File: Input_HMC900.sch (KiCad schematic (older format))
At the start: 8 parts

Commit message: As implemented for v1
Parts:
- R23: value 0 -> 0(NP)
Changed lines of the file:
@@
 AR Path="/60D21B6E/61121120/60F9EBFF" Ref="C28"  Part="1"
 AR Path="/60D21B6E/60F52DEE/60F9EBFF" Ref="C30"  Part="1"
-F 0 "C30" H 6150 2800 50  0000 R CNN
+F 0 "C28" H 6150 2800 50  0000 R CNN
 F 1 "100p" H 6175 3000 50  0000 R CNN
 F 2 "Capacitor_SMD:C_0603_1608Metric_Pad1.08x0.95mm_HandSolder" H 6238 2750 50  0001 C CNN
@@
 AR Path="/60D21B6E/61121120/60F9EC14" Ref="#PWR0131"  Part="1"
 AR Path="/60D21B6E/60F52DEE/60F9EC14" Ref="#PWR0135"  Part="1"
-F 0 "#PWR0135" H 6200 2850 50  0001 C CNN
+F 0 "#PWR0131" H 6200 2850 50  0001 C CNN
 F 1 "GND" H 6205 2927 50  0000 C CNN
 F 2 "" H 6200 3100 50  0001 C CNN
@@
 AR Path="/60D21B6E/61121120/60F9EC05" Ref="C29"  Part="1"
 AR Path="/60D21B6E/60F52DEE/60F9EC05" Ref="C31"  Part="1"
-F 0 "C31" H 6450 2800 50  0000 R CNN
+F 0 "C29" H 6450 2800 50  0000 R CNN
 F 1 "100p" H 6475 3000 50  0000 R CNN
 F 2 "Capacitor_SMD:C_0603_1608Metric_Pad1.08x0.95mm_HandSolder" H 6538 2750 50  0001 C CNN
@@
 AR Path="/60D21B6E/61121120/6100BC4B" Ref="#PWR0134"  Part="1"
 AR Path="/60D21B6E/60F52DEE/6100BC4B" Ref="#PWR0136"  Part="1"
-F 0 "#PWR0136" H 6500 2850 50  0001 C CNN
+F 0 "#PWR0134" H 6500 2850 50  0001 C CNN
 F 1 "GND" H 6505 2927 50  0000 C CNN
 F 2 "" H 6500 3100 50  0001 C CNN
@@
 AR Path="/60D21B6E/61121120/60F9EBF5" Ref="R32"  Part="1"
 AR Path="/60D21B6E/60F52DEE/60F9EBF5" Ref="R33"  Part="1"
-F 0 "R33" H 5920 2946 50  0000 L CNN
+F 0 "R32" H 5920 2946 50  0000 L CNN
 F 1 "51" H 5920 2855 50  0000 L CNN
 F 2 "Resistor_SMD:R_0603_1608Metric_Pad0.98x0.95mm_HandSolder" V 5780 2900 50  0001 C CNN
@@
 AR Path="/60D21B6E/61121120/60F9EC23" Ref="R31"  Part="1"
 AR Path="/60D21B6E/60F52DEE/60F9EC23" Ref="R34"  Part="1"
-F 0 "R34" H 5620 2946 50  0000 L CNN
+F 0 "R31" H 5620 2946 50  0000 L CNN
 F 1 "51" H 5620 2855 50  0000 L CNN
 F 2 "Resistor_SMD:R_0603_1608Metric_Pad0.98x0.95mm_HandSolder" V 5480 2900 50  0001 C CNN
@@
 AR Path="/60D21B6E/61121120/60F9EC42" Ref="#PWR0133"  Part="1"
 AR Path="/60D21B6E/60F52DEE/60F9EC42" Ref="#PWR0137"  Part="1"
-F 0 "#PWR0137" H 4900 3650 50  0001 C CNN
+F 0 "#PWR0133" H 4900 3650 50  0001 C CNN
 F 1 "GND" H 4905 3727 50  0000 C CNN
 F 2 "" H 4900 3900 50  0001 C CNN
@@
 AR Path="/60D21B6E/61121120/60F9EC6C" Ref="C45"  Part="1"
 AR Path="/60D21B6E/60F52DEE/60F9EC6C" Ref="C46"  Part="1"
-F 0 "C46" H 4785 3654 50  0000 R CNN
+F 0 "C45" H 4785 3654 50  0000 R CNN
 F 1 "10µ" H 4785 3745 50  0000 R CNN
 F 2 "Capacitor_SMD:C_0603_1608Metric_Pad1.08x0.95mm_HandSolder" H 4938 3550 50  0001 C CNN
@@
 AR Path="/60D21B6E/60F52DEE/60F9EC66" Ref="TR4"  Part="1"
 AR Path="/60F9EC66" Ref="TR4"  Part="1"
-F 0 "TR4" H 4250 3881 50  0000 C CNN
+F 0 "TR3" H 4250 3881 50  0000 C CNN
 F 1 "ADT2-1T" H 4250 3790 50  0000 C CNN
 F 2 "RF_Mini-Circuits:Mini-Circuits_CD542_H2.84mm" H 4250 3150 50  0001 C CNN
@@
 AR Path="/60D21B6E/61121120/614655FD" Ref="R23"  Part="1"
 AR Path="/60D21B6E/60F52DEE/614655FD" Ref="R26"  Part="1"
-F 0 "R26" H 3870 3346 50  0000 L CNN
-F 1 "0" V 3800 3250 50  0000 L CNN
+F 0 "R23" H 3870 3346 50  0000 L CNN
+F 1 "0(NP)" V 3800 3200 50  0000 L CNN
 F 2 "Resistor_SMD:R_0603_1608Metric_Pad0.98x0.95mm_HandSolder" V 3730 3300 50  0001 C CNN
 F 3 "~" H 3800 3300 50  0001 C CNN
@@
 AR Path="/60D21B6E/61121120/6147240B" Ref="R22"  Part="1"
 AR Path="/60D21B6E/60F52DEE/6147240B" Ref="R25"  Part="1"
-F 0 "R25" H 4070 3146 50  0000 L CNN
+F 0 "R22" H 4070 3146 50  0000 L CNN
 F 1 "0" V 4000 3050 50  0000 L CNN
 F 2 "Resistor_SMD:R_0603_1608Metric_Pad0.98x0.95mm_HandSolder" V 3930 3100 50  0001 C CNN
@@
 AR Path="/60D21B6E/61121120/614747AB" Ref="#PWR09"  Part="1"
 AR Path="/60D21B6E/60F52DEE/614747AB" Ref="#PWR010"  Part="1"
-F 0 "#PWR010" H 3800 2750 50  0001 C CNN
+F 0 "#PWR09" H 3800 2750 50  0001 C CNN
 F 1 "GND" H 3805 2827 50  0000 C CNN
 F 2 "" H 3800 3000 50  0001 C CNN

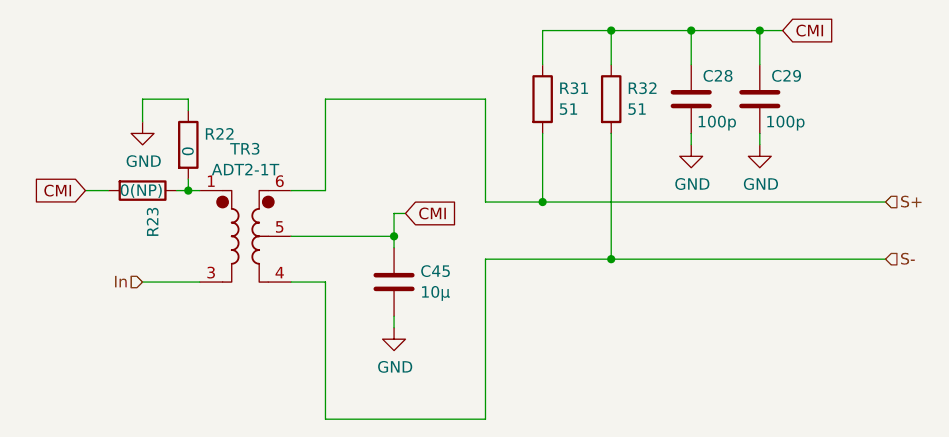
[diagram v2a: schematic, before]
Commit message: removed unused options added aop at the output
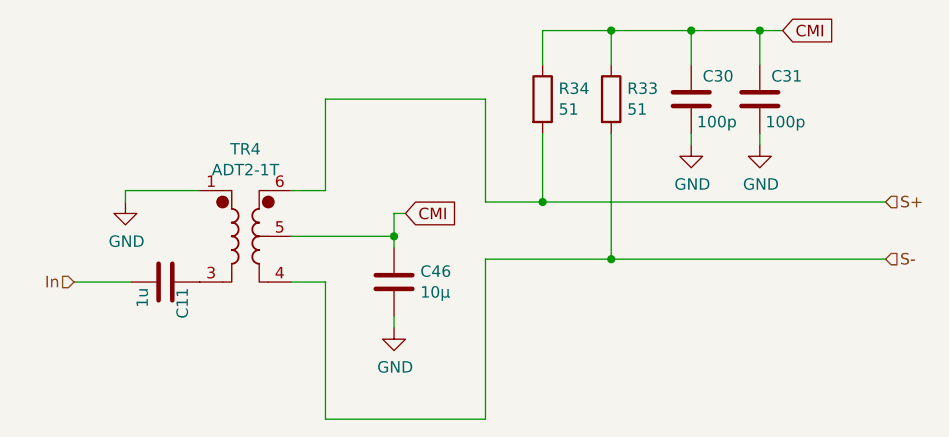
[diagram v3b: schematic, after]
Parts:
- removed R22: 0, Resistor_SMD:R_0603_1608Metric_Pad0.98x0.95mm_HandSolder, symbol Device:R
- removed R23: 0(NP), Resistor_SMD:R_0603_1608Metric_Pad0.98x0.95mm_HandSolder, symbol Device:R
- added C10: 1u, Capacitor_SMD:C_0603_1608Metric_Pad1.08x0.95mm_HandSolder, symbol Device:C
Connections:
- net GND: now also TR4.1
- net In: now also C10.1; no longer TR4.3
- new net: C10.2, TR4.3
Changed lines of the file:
@@
 AR Path="/60D21B6E/61121120/60F9EBFF" Ref="C28"  Part="1"
 AR Path="/60D21B6E/60F52DEE/60F9EBFF" Ref="C30"  Part="1"
-F 0 "C28" H 6150 2800 50  0000 R CNN
+F 0 "C30" H 6150 2800 50  0000 R CNN
 F 1 "100p" H 6175 3000 50  0000 R CNN
 F 2 "Capacitor_SMD:C_0603_1608Metric_Pad1.08x0.95mm_HandSolder" H 6238 2750 50  0001 C CNN
@@
 AR Path="/60D21B6E/61121120/60F9EC14" Ref="#PWR0131"  Part="1"
 AR Path="/60D21B6E/60F52DEE/60F9EC14" Ref="#PWR0135"  Part="1"
-F 0 "#PWR0131" H 6200 2850 50  0001 C CNN
+F 0 "#PWR0135" H 6200 2850 50  0001 C CNN
 F 1 "GND" H 6205 2927 50  0000 C CNN
 F 2 "" H 6200 3100 50  0001 C CNN
@@
 AR Path="/60D21B6E/61121120/60F9EC05" Ref="C29"  Part="1"
 AR Path="/60D21B6E/60F52DEE/60F9EC05" Ref="C31"  Part="1"
-F 0 "C29" H 6450 2800 50  0000 R CNN
+F 0 "C31" H 6450 2800 50  0000 R CNN
 F 1 "100p" H 6475 3000 50  0000 R CNN
 F 2 "Capacitor_SMD:C_0603_1608Metric_Pad1.08x0.95mm_HandSolder" H 6538 2750 50  0001 C CNN
@@
 AR Path="/60D21B6E/61121120/6100BC4B" Ref="#PWR0134"  Part="1"
 AR Path="/60D21B6E/60F52DEE/6100BC4B" Ref="#PWR0136"  Part="1"
-F 0 "#PWR0134" H 6500 2850 50  0001 C CNN
+F 0 "#PWR0136" H 6500 2850 50  0001 C CNN
 F 1 "GND" H 6505 2927 50  0000 C CNN
 F 2 "" H 6500 3100 50  0001 C CNN
@@
 Wire Wire Line
 	5850 3600 7050 3600
-Text HLabel 3800 3700 0    50   Input ~ 0
+Text HLabel 3500 3700 0    50   Input ~ 0
 In
 Text HLabel 7050 3350 2    50   Input ~ 0
@@
 AR Path="/60D21B6E/61121120/60F9EBF5" Ref="R32"  Part="1"
 AR Path="/60D21B6E/60F52DEE/60F9EBF5" Ref="R33"  Part="1"
-F 0 "R32" H 5920 2946 50  0000 L CNN
+F 0 "R33" H 5920 2946 50  0000 L CNN
 F 1 "51" H 5920 2855 50  0000 L CNN
 F 2 "Resistor_SMD:R_0603_1608Metric_Pad0.98x0.95mm_HandSolder" V 5780 2900 50  0001 C CNN
@@
 AR Path="/60D21B6E/61121120/60F9EC23" Ref="R31"  Part="1"
 AR Path="/60D21B6E/60F52DEE/60F9EC23" Ref="R34"  Part="1"
-F 0 "R31" H 5620 2946 50  0000 L CNN
+F 0 "R34" H 5620 2946 50  0000 L CNN
 F 1 "51" H 5620 2855 50  0000 L CNN
 F 2 "Resistor_SMD:R_0603_1608Metric_Pad0.98x0.95mm_HandSolder" V 5480 2900 50  0001 C CNN
@@
 AR Path="/60D21B6E/61121120/60F9EC42" Ref="#PWR0133"  Part="1"
 AR Path="/60D21B6E/60F52DEE/60F9EC42" Ref="#PWR0137"  Part="1"
-F 0 "#PWR0133" H 4900 3650 50  0001 C CNN
+F 0 "#PWR0137" H 4900 3650 50  0001 C CNN
 F 1 "GND" H 4905 3727 50  0000 C CNN
 F 2 "" H 4900 3900 50  0001 C CNN
@@
 Wire Wire Line
 	4900 3500 4900 3550
-Wire Wire Line
-	4050 3300 4000 3300
 $Comp
 L Device:C C?
@@
 AR Path="/60D21B6E/61121120/60F9EC6C" Ref="C45"  Part="1"
 AR Path="/60D21B6E/60F52DEE/60F9EC6C" Ref="C46"  Part="1"
-F 0 "C45" H 4785 3654 50  0000 R CNN
+F 0 "C46" H 4785 3654 50  0000 R CNN
 F 1 "10µ" H 4785 3745 50  0000 R CNN
 F 2 "Capacitor_SMD:C_0603_1608Metric_Pad1.08x0.95mm_HandSolder" H 4938 3550 50  0001 C CNN
@@
 AR Path="/60D21B6E/60F52DEE/60F9EC66" Ref="TR4"  Part="1"
 AR Path="/60F9EC66" Ref="TR4"  Part="1"
-F 0 "TR3" H 4250 3881 50  0000 C CNN
+F 0 "TR4" H 4250 3881 50  0000 C CNN
 F 1 "ADT2-1T" H 4250 3790 50  0000 C CNN
 F 2 "RF_Mini-Circuits:Mini-Circuits_CD542_H2.84mm" H 4250 3150 50  0001 C CNN
@@
 Connection ~ 5550 3350
 Wire Wire Line
-	3800 3700 4050 3700
+	3500 3700 3750 3700
 Wire Wire Line
 	4450 3300 4600 3300
@@
 Wire Wire Line
 	4600 4300 5300 4300
-Text GLabel 3550 3300 0    50   Input ~ 0
-CMI
-$Comp
-L Device:R R?
-U 1 1 614655FD
-P 3800 3300
-AR Path="/60D21B6E/614655FD" Ref="R?"  Part="1"
-AR Path="/60D21B6E/60D894BC/614655FD" Ref="R?"  Part="1"
-AR Path="/60D21B6E/6110419F/614655FD" Ref="R?"  Part="1"
-AR Path="/60D21B6E/61121120/614655FD" Ref="R23"  Part="1"
-AR Path="/60D21B6E/60F52DEE/614655FD" Ref="R26"  Part="1"
-F 0 "R23" H 3870 3346 50  0000 L CNN
-F 1 "0(NP)" V 3800 3200 50  0000 L CNN
-F 2 "Resistor_SMD:R_0603_1608Metric_Pad0.98x0.95mm_HandSolder" V 3730 3300 50  0001 C CNN
-F 3 "~" H 3800 3300 50  0001 C CNN
-	1    3800 3300
-	0    1    1    0
-$EndComp
-Wire Wire Line
-	3650 3300 3550 3300
-$Comp
-L Device:R R?
-U 1 1 6147240B
-P 4000 3100
-AR Path="/60D21B6E/6147240B" Ref="R?"  Part="1"
-AR Path="/60D21B6E/60D894BC/6147240B" Ref="R?"  Part="1"
-AR Path="/60D21B6E/6110419F/6147240B" Ref="R?"  Part="1"
-AR Path="/60D21B6E/61121120/6147240B" Ref="R22"  Part="1"
-AR Path="/60D21B6E/60F52DEE/6147240B" Ref="R25"  Part="1"
-F 0 "R22" H 4070 3146 50  0000 L CNN
-F 1 "0" V 4000 3050 50  0000 L CNN
-F 2 "Resistor_SMD:R_0603_1608Metric_Pad0.98x0.95mm_HandSolder" V 3930 3100 50  0001 C CNN
-F 3 "~" H 4000 3100 50  0001 C CNN
-	1    4000 3100
-	1    0    0    -1
-$EndComp
 $Comp
 L power:GND #PWR?
 U 1 1 614747AB
-P 3800 3000
+P 3725 3350
 AR Path="/60D21B6E/614747AB" Ref="#PWR?"  Part="1"
 AR Path="/60D21B6E/60D894BC/614747AB" Ref="#PWR?"  Part="1"
@@
 AR Path="/60D21B6E/61121120/614747AB" Ref="#PWR09"  Part="1"
 AR Path="/60D21B6E/60F52DEE/614747AB" Ref="#PWR010"  Part="1"
-F 0 "#PWR09" H 3800 2750 50  0001 C CNN
-F 1 "GND" H 3805 2827 50  0000 C CNN
-F 2 "" H 3800 3000 50  0001 C CNN
-F 3 "" H 3800 3000 50  0001 C CNN
-	1    3800 3000
-	1    0    0    -1
-$EndComp
-Wire Wire Line
-	3800 2900 4000 2900
-Wire Wire Line
-	4000 2900 4000 2950
-Wire Wire Line
-	3800 2900 3800 3000
-Wire Wire Line
-	4000 3250 4000 3300
-Connection ~ 4000 3300
-Wire Wire Line
-	4000 3300 3950 3300
+F 0 "#PWR010" H 3725 3100 50  0001 C CNN
+F 1 "GND" H 3730 3177 50  0000 C CNN
+F 2 "" H 3725 3350 50  0001 C CNN
+F 3 "" H 3725 3350 50  0001 C CNN
+	1    3725 3350
+	1    0    0    -1
+$EndComp
+Wire Wire Line
+	3725 3300 3725 3350
+Wire Wire Line
+	3725 3300 4050 3300
+$Comp
+L Device:C C?
+U 1 1 616D127D
+P 3900 3700
+AR Path="/60D21B6E/616D127D" Ref="C?"  Part="1"
+AR Path="/616D127D" Ref="C?"  Part="1"
+AR Path="/60D21B6E/61121120/616D127D" Ref="C10"  Part="1"
+AR Path="/60D21B6E/60F52DEE/616D127D" Ref="C11"  Part="1"
+F 0 "C11" H 3875 3625 50  0000 R CNN
+F 1 "1u" H 3875 3800 50  0000 R CNN
+F 2 "Capacitor_SMD:C_0603_1608Metric_Pad1.08x0.95mm_HandSolder" H 3938 3550 50  0001 C CNN
+F 3 "~" H 3900 3700 50  0001 C CNN
+	1    3900 3700
+	0    -1   -1   0
+$EndComp
 $EndSCHEMATC

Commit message: Made the 2 DS1085 signals merge before the filter Looped the filter's 1st output to the now liberated 2nd input to double the filtration Added a protection diode before the filter
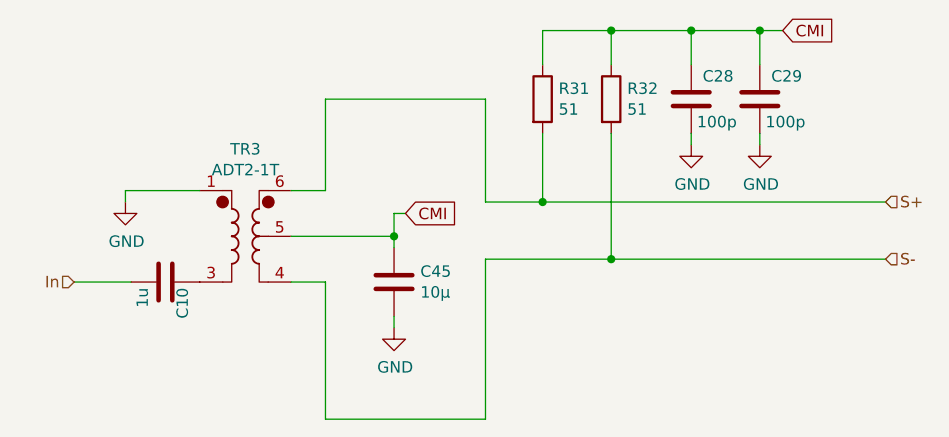
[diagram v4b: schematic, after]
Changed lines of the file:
@@
 $Descr A4 11693 8268
 encoding utf-8
-Sheet 4 7
+Sheet 3 5
 Title ""
 Date ""
@@
 AR Path="/60D21B6E/61121120/60F9EBFF" Ref="C28"  Part="1"
 AR Path="/60D21B6E/60F52DEE/60F9EBFF" Ref="C30"  Part="1"
-F 0 "C30" H 6150 2800 50  0000 R CNN
+F 0 "C28" H 6150 2800 50  0000 R CNN
 F 1 "100p" H 6175 3000 50  0000 R CNN
 F 2 "Capacitor_SMD:C_0603_1608Metric_Pad1.08x0.95mm_HandSolder" H 6238 2750 50  0001 C CNN
@@
 AR Path="/60D21B6E/61121120/60F9EC14" Ref="#PWR0131"  Part="1"
 AR Path="/60D21B6E/60F52DEE/60F9EC14" Ref="#PWR0135"  Part="1"
-F 0 "#PWR0135" H 6200 2850 50  0001 C CNN
+F 0 "#PWR0131" H 6200 2850 50  0001 C CNN
 F 1 "GND" H 6205 2927 50  0000 C CNN
 F 2 "" H 6200 3100 50  0001 C CNN
@@
 AR Path="/60D21B6E/61121120/60F9EC05" Ref="C29"  Part="1"
 AR Path="/60D21B6E/60F52DEE/60F9EC05" Ref="C31"  Part="1"
-F 0 "C31" H 6450 2800 50  0000 R CNN
+F 0 "C29" H 6450 2800 50  0000 R CNN
 F 1 "100p" H 6475 3000 50  0000 R CNN
 F 2 "Capacitor_SMD:C_0603_1608Metric_Pad1.08x0.95mm_HandSolder" H 6538 2750 50  0001 C CNN
@@
 AR Path="/60D21B6E/61121120/6100BC4B" Ref="#PWR0134"  Part="1"
 AR Path="/60D21B6E/60F52DEE/6100BC4B" Ref="#PWR0136"  Part="1"
-F 0 "#PWR0136" H 6500 2850 50  0001 C CNN
+F 0 "#PWR0134" H 6500 2850 50  0001 C CNN
 F 1 "GND" H 6505 2927 50  0000 C CNN
 F 2 "" H 6500 3100 50  0001 C CNN
@@
 AR Path="/60D21B6E/61121120/60F9EBF5" Ref="R32"  Part="1"
 AR Path="/60D21B6E/60F52DEE/60F9EBF5" Ref="R33"  Part="1"
-F 0 "R33" H 5920 2946 50  0000 L CNN
+F 0 "R32" H 5920 2946 50  0000 L CNN
 F 1 "51" H 5920 2855 50  0000 L CNN
 F 2 "Resistor_SMD:R_0603_1608Metric_Pad0.98x0.95mm_HandSolder" V 5780 2900 50  0001 C CNN
@@
 AR Path="/60D21B6E/61121120/60F9EC23" Ref="R31"  Part="1"
 AR Path="/60D21B6E/60F52DEE/60F9EC23" Ref="R34"  Part="1"
-F 0 "R34" H 5620 2946 50  0000 L CNN
+F 0 "R31" H 5620 2946 50  0000 L CNN
 F 1 "51" H 5620 2855 50  0000 L CNN
 F 2 "Resistor_SMD:R_0603_1608Metric_Pad0.98x0.95mm_HandSolder" V 5480 2900 50  0001 C CNN
@@
 AR Path="/60D21B6E/61121120/60F9EC42" Ref="#PWR0133"  Part="1"
 AR Path="/60D21B6E/60F52DEE/60F9EC42" Ref="#PWR0137"  Part="1"
-F 0 "#PWR0137" H 4900 3650 50  0001 C CNN
+F 0 "#PWR0133" H 4900 3650 50  0001 C CNN
 F 1 "GND" H 4905 3727 50  0000 C CNN
 F 2 "" H 4900 3900 50  0001 C CNN
@@
 AR Path="/60D21B6E/61121120/60F9EC6C" Ref="C45"  Part="1"
 AR Path="/60D21B6E/60F52DEE/60F9EC6C" Ref="C46"  Part="1"
-F 0 "C46" H 4785 3654 50  0000 R CNN
+F 0 "C45" H 4785 3654 50  0000 R CNN
 F 1 "10µ" H 4785 3745 50  0000 R CNN
 F 2 "Capacitor_SMD:C_0603_1608Metric_Pad1.08x0.95mm_HandSolder" H 4938 3550 50  0001 C CNN
@@
 AR Path="/60D21B6E/60F52DEE/60F9EC66" Ref="TR4"  Part="1"
 AR Path="/60F9EC66" Ref="TR4"  Part="1"
-F 0 "TR4" H 4250 3881 50  0000 C CNN
+F 0 "TR3" H 4250 3881 50  0000 C CNN
 F 1 "ADT2-1T" H 4250 3790 50  0000 C CNN
 F 2 "RF_Mini-Circuits:Mini-Circuits_CD542_H2.84mm" H 4250 3150 50  0001 C CNN
@@
 AR Path="/60D21B6E/61121120/614747AB" Ref="#PWR09"  Part="1"
 AR Path="/60D21B6E/60F52DEE/614747AB" Ref="#PWR010"  Part="1"
-F 0 "#PWR010" H 3725 3100 50  0001 C CNN
+F 0 "#PWR09" H 3725 3100 50  0001 C CNN
 F 1 "GND" H 3730 3177 50  0000 C CNN
 F 2 "" H 3725 3350 50  0001 C CNN
@@
 AR Path="/60D21B6E/61121120/616D127D" Ref="C10"  Part="1"
 AR Path="/60D21B6E/60F52DEE/616D127D" Ref="C11"  Part="1"
-F 0 "C11" H 3875 3625 50  0000 R CNN
+F 0 "C10" H 3875 3625 50  0000 R CNN
 F 1 "1u" H 3875 3800 50  0000 R CNN
 F 2 "Capacitor_SMD:C_0603_1608Metric_Pad1.08x0.95mm_HandSolder" H 3938 3550 50  0001 C CNN
